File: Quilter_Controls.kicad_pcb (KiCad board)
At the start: 2 copper layers, 40.4 x 110 mm, 16 parts, among them J1 Conn_01x10_Male, J10 Conn_01x04_Male, J2 Conn_01x10_Male, J3 Conn_01x10_Male, J4 Audio_In, J5 Audio_Out, J6 Audio_Mix, J7 Freq_V_Oct, J8 Freq_CV, J9 Conn_02x04_Top_Bottom

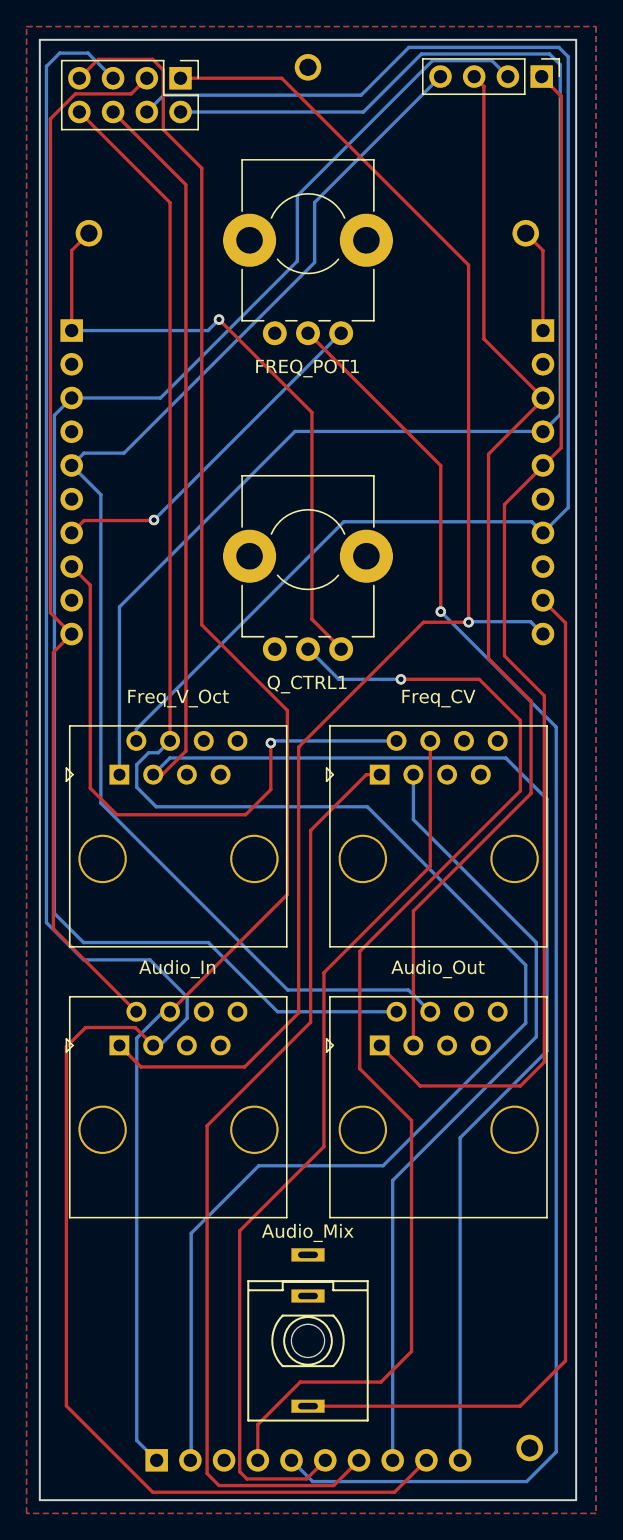
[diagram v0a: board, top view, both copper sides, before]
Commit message: Re-routed Controls board
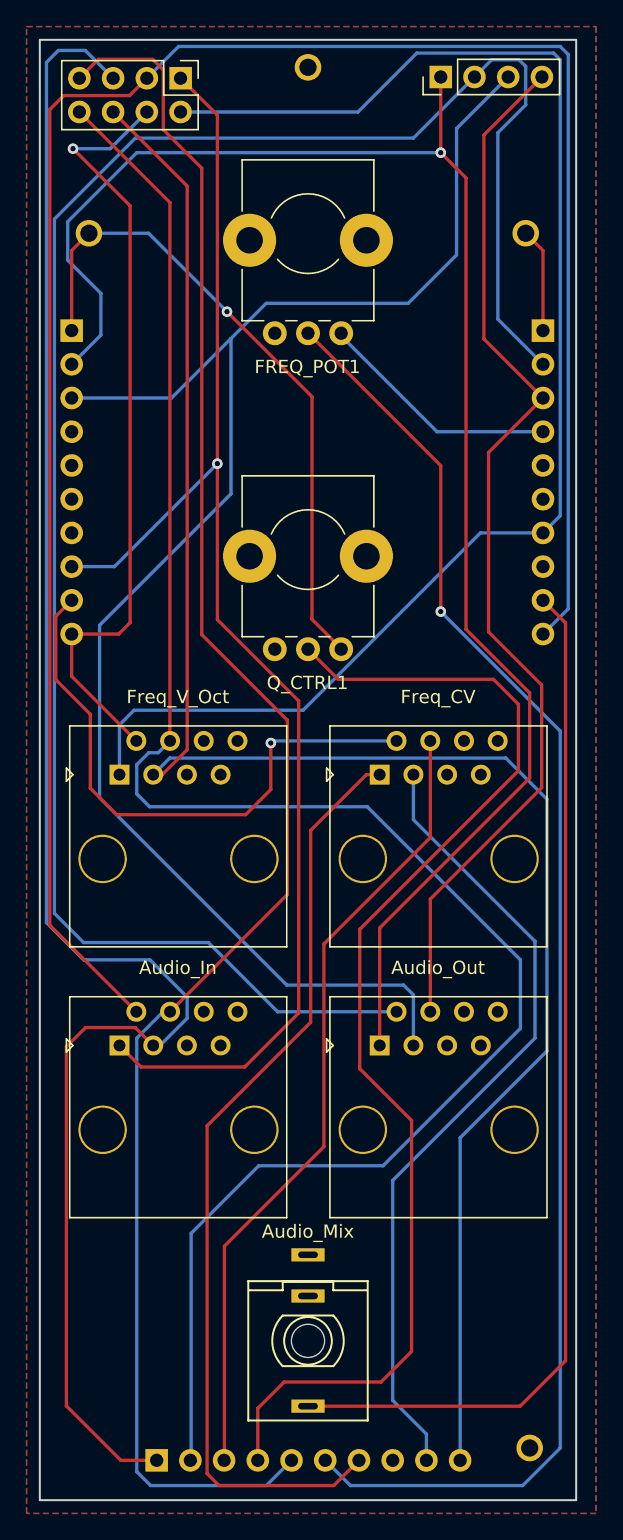
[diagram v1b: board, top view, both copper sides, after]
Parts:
- moved J10 7.60 mm to (80.2, 43.7), turned to 90 degrees
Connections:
- J1 pad 10: /AUDIO_IN1 -> /AUDIO_IN2
- J1 pad 2: unconnected-(J1-Pad2) -> /AUDIO_BUFF2
- J1 pad 3: /AUDIO_BUFF3 -> /AUDIO_BUFF4
- J1 pad 4: /FREQ_V_OCT1 -> /FREQ_POT_5V
- J1 pad 5: /AUDIO_BUFF1 -> unconnected-(J1-Pad5)
- J1 pad 7: /FREQ_V_OCT2 -> /FREQ_V_OCT1
- J2 pad 10: /AUDIO_IN2 -> /FREQ_V_OCT2
- J2 pad 2: unconnected-(J2-Pad2) -> /AUDIO_BUFF1
- J2 pad 3: /AUDIO_BUFF2 -> /AUDIO_BUFF3
- J2 pad 5: /AUDIO_BUFF4 -> unconnected-(J2-Pad5)
- J2 pad 7: /FREQ_POT_5V -> unconnected-(J2-Pad7)
- J2 pad 8: /FREQ_CV2 -> /AUDIO_IN1
- J2 pad 9: unconnected-(J2-Pad9) -> /FREQ_CV2
- J3 pad 1: /AUDIO_IN4 -> /AUDIO_IN3
- J3 pad 3: unconnected-(J3-Pad3) -> /FREQ_CV4
- J3 pad 5: /FREQ_POT -> /AUDIO_IN4
- J3 pad 6: /FREQ_CV4 -> /FREQ_POT
- J3 pad 8: /FREQ_CV3 -> unconnected-(J3-Pad8)
- J3 pad 9: /AUDIO_IN3 -> /FREQ_CV3
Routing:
- net /AUDIO_IN2: track 79.6 -> 156.4 mm
- net /FREQ_V_OCT2: track 109.0 -> 59.0 mm, vias 0 -> 1
- net /AUDIO_BUFF3: track 81.8 -> 120.8 mm
- net /AUDIO_BUFF2: track 115.0 -> 146.5 mm
- net /AUDIO_BUFF1: track 92.3 -> 123.3 mm, vias 0 -> 1
- net /AUDIO_IN3: track 154.2 -> 132.2 mm
- net /AUDIO_BUFF4: track 100.2 -> 80.9 mm
- net /AUDIO_IN4: track 121.5 -> 134.6 mm
- net /AUDIO_IN1: track 113.0 -> 104.1 mm
- net /FREQ_POT_5V: track 26.5 -> 18.4 mm, vias 1 -> 0
- net /FREQ_CV4: track 68.2 -> 60.6 mm
- net /FREQ_POT: track 113.6 -> 111.5 mm
- net +12V: track 47.9 -> 49.6 mm
- net /FREQ_CV2: track 45.5 -> 44.0 mm
- net /Q_POT: track 89.0 -> 90.2 mm, vias 1 -> 0
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
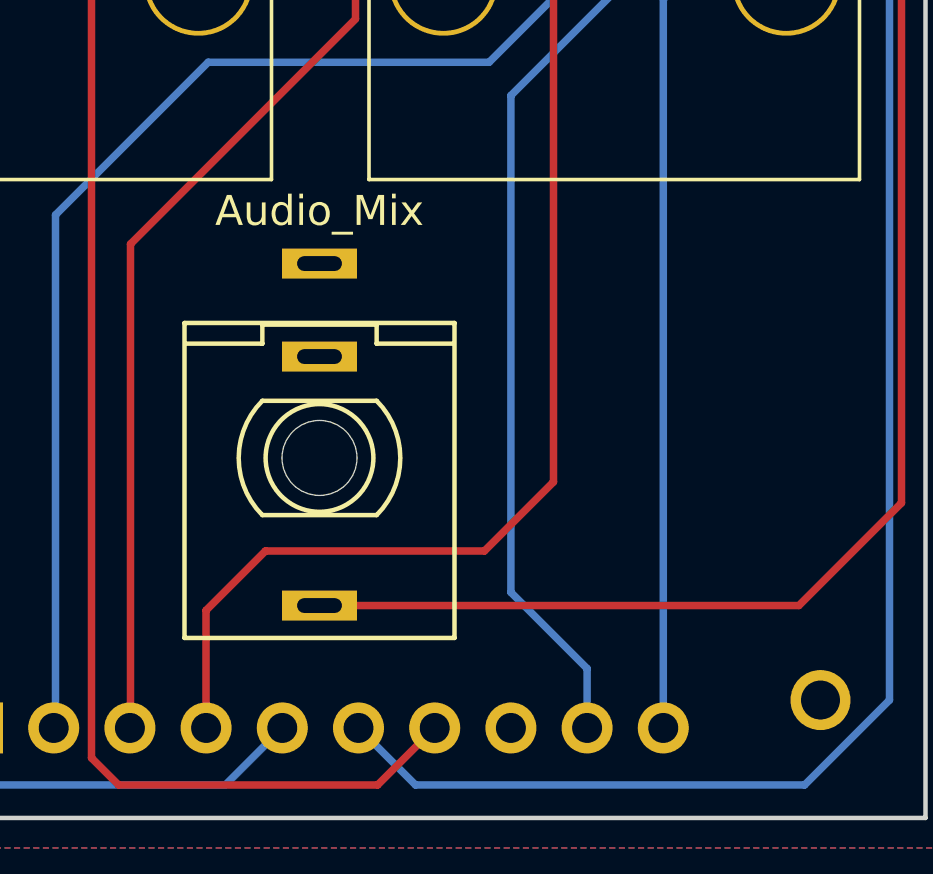
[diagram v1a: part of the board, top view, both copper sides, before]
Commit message: Added all voice filter CV; panel draft done
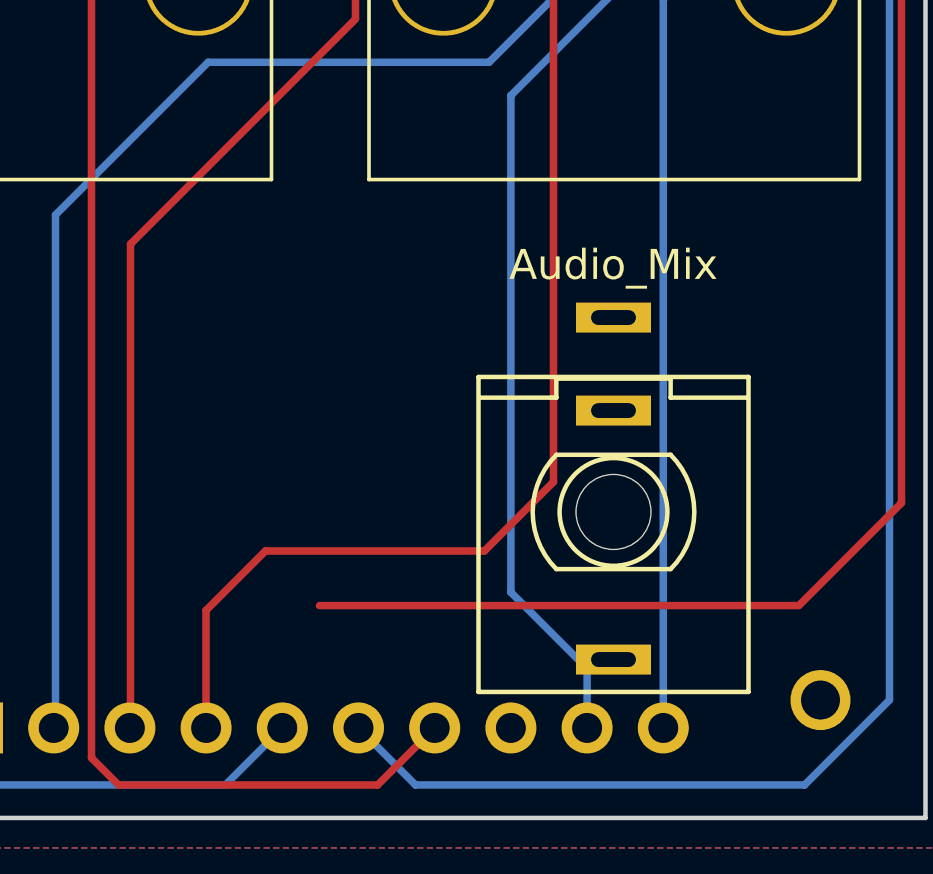
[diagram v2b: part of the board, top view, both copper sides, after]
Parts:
- moved J6 9.96 mm to (80.0, 140.7)
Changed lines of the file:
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@@
   )
   (footprint "Custom_Footprints:THONKICONN_hole" (layer "F.Cu")
-    (at 70.2 138.9 180)
+    (at 80 140.7 180)
     (property "Sheetfile" "Quilter_Controls.kicad_sch")
     (property "Sheetname" "")

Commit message: Updates to panel and component boards
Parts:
- added J11: Freq_In, Custom_Footprints:THONKICONN_hole, F.Cu at (60.4, 140.6)
- J10, J9: moved to B.Cu
- moved J8 30.4 mm to (60.4, 124.1)
- moved J4 26.2 mm to (80.0, 103.9)
- moved Q_CTRL1 10.2 mm to (80.0, 76.6)
- moved FREQ_POT1 5.54 mm to (65.0, 53.6)
- moved J7 3.00 mm to (60.4, 103.9)
- moved J5 2.80 mm to (80.0, 124.1)
- moved J9 2.58 mm to (60.6, 46.4), turned to 90 degrees
- moved J6 0.10 mm to (80.0, 140.6), turned to -90 degrees
- turned J10 to -90 degrees
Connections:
- J3 pad 8: unconnected-(J3-Pad8) -> /FREQ_JACK
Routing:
- net /FREQ_V_OCT3: track 137.7 -> 64.2 mm
- net /AUDIO_IN2: track 156.4 -> 94.4 mm
- net /AUDIO_IN1: track 104.1 -> 45.4 mm, vias 1 -> 0
- net +12V: track 49.6 -> 7.87 mm, vias 1 -> 0
- net /FREQ_CV1: track 71.2 -> 35.9 mm
- net /FREQ_CV4: track 60.6 -> 35.9 mm
- net /FREQ_V_OCT4: track 143.2 -> 118.7 mm
- net /FREQ_CV3: track 60.9 -> 37.0 mm
- net /FREQ_V_OCT1: track 108.5 -> 128.6 mm
- net /Q_POT: track 90.2 -> 70.3 mm
- net /AUDIO_MIX: track 78.8 -> 61.1 mm
- net /FREQ_JACK: track 0.00 -> 16.0 mm
- net /FREQ_CV2: track 44.0 -> 35.8 mm, vias 1 -> 0
- net /AUDIO_BUFF2: track 146.5 -> 153.4 mm
- net /FREQ_POT_5V: track 18.4 -> 24.3 mm
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
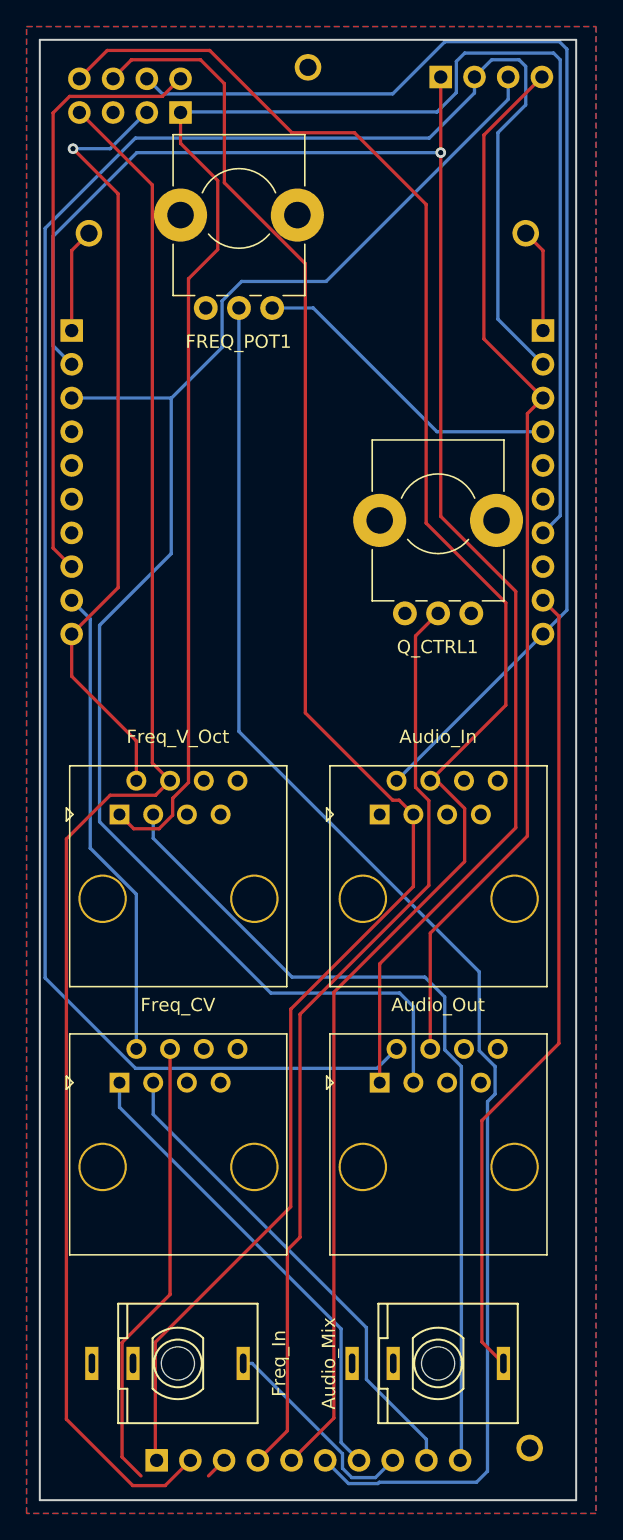
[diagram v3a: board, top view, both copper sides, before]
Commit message: Finished routing components and controls
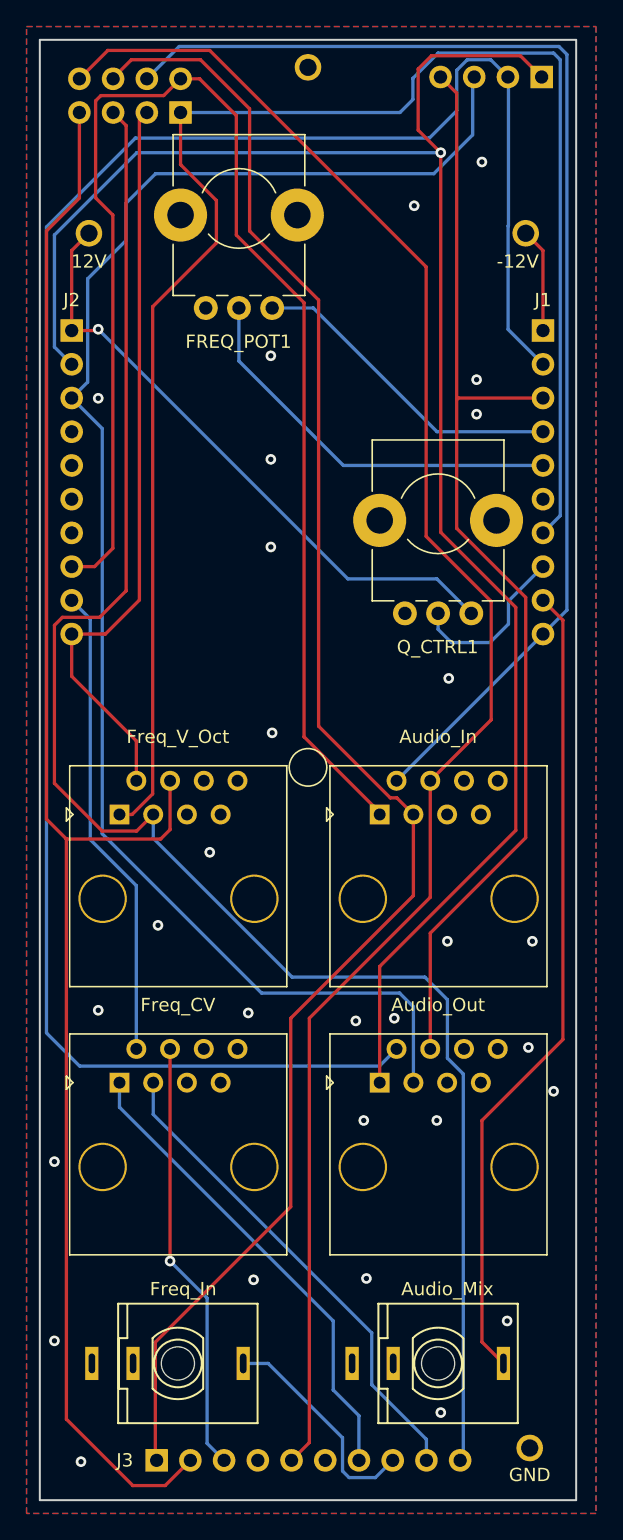
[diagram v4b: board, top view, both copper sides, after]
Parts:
- added D1: 3d_Model_Panel, Custom_Footprints:3D_Dummy, B.Cu at (70.2, 100.0)
- added D2: 3d_Model_Components, Custom_Footprints:3D_Dummy, F.Cu at (70.2, 95.7)
- moved J10 7.60 mm to (87.8, 43.7), turned to 90 degrees
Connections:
- J1 pad 5: unconnected-(J1-Pad5) -> /FREQ_POT
- J1 pad 8: unconnected-(J1-Pad8) -> /Q_POT
- J2 pad 4: unconnected-(J2-Pad4) -> GND
- J2 pad 5: unconnected-(J2-Pad5) -> GND
- J2 pad 7: unconnected-(J2-Pad7) -> GND
- J3 pad 4: /Q_POT -> GND
- J3 pad 6: /FREQ_POT -> GND
- J9 pad 1: /AUDIO_IN1 -> /FREQ_V_OCT1
- J9 pad 2: /FREQ_V_OCT1 -> /AUDIO_IN1
- J9 pad 3: /AUDIO_IN2 -> /FREQ_V_OCT2
- J9 pad 4: /FREQ_V_OCT2 -> /AUDIO_IN2
- J9 pad 5: /AUDIO_IN3 -> /FREQ_V_OCT3
- J9 pad 6: /FREQ_V_OCT3 -> /AUDIO_IN3
- J9 pad 7: /AUDIO_IN4 -> /FREQ_V_OCT4
- J9 pad 8: /FREQ_V_OCT4 -> /AUDIO_IN4
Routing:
- net /FREQ_POT: track 109.2 -> 30.2 mm
- net /FREQ_V_OCT3: track 64.2 -> 128.5 mm
- net /AUDIO_IN1: track 45.4 -> 107.5 mm
- net /Q_POT: track 70.3 -> 12.9 mm
- net +12V: track 7.87 -> 46.9 mm, vias 0 -> 1
- net /AUDIO_BUFF1: track 124.4 -> 136.0 mm
- net /AUDIO_IN4: track 138.0 -> 131.9 mm
- net /FREQ_V_OCT4: track 118.7 -> 124.1 mm
- net /AUDIO_BUFF4: track 80.4 -> 85.4 mm
- net /FREQ_V_OCT1: track 128.6 -> 125.4 mm
- net /FREQ_CV4: track 35.9 -> 32.7 mm, vias 0 -> 1
- net /FREQ_V_OCT2: track 59.2 -> 56.2 mm, vias 1 -> 0
- net /AUDIO_BUFF3: track 115.2 -> 117.3 mm
- net /AUDIO_IN2: track 94.4 -> 92.9 mm
- net /FREQ_JACK: track 16.0 -> 16.8 mm
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- added copper zone on B.Cu, net GND
- added copper zone on F.Cu, net GND
- removed copper zone on B.Cu, net (none)
- removed copper zone on F.Cu, net (none)
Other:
- board text added: "-12V"
- board text added: "1"
- board text added: "12V"
- board text added: "GND"
- board text added: "In"
- board text added: "J1"
- board text added: "J2"
- board text added: "J3"
- board text added: "Out"
- board text added: "V/O"

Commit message: Schematic formatting
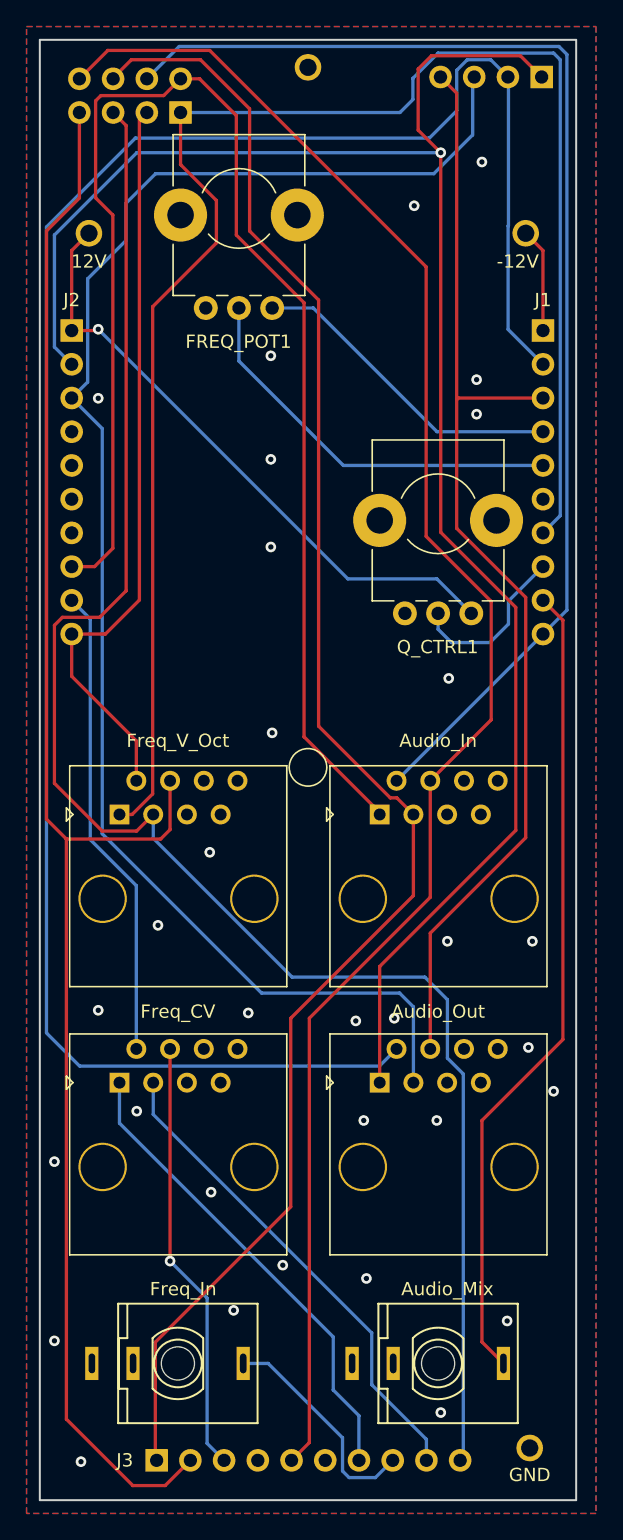
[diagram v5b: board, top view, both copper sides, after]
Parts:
- D1: value 3d_Model_Panel -> 3d_Model_Components
- D2: value 3d_Model_Components -> 3d_Model_Panel
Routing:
- net GND: vias 29 -> 32
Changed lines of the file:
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@@
       (effects (font (size 1 1) (thickness 0.15)))
     )
-    (fp_text value "3d_Model_Components" (at 0 -3 unlocked) (layer "F.Fab")
+    (fp_text value "3d_Model_Panel" (at 0 -3 unlocked) (layer "F.Fab")
       (effects (font (size 1 1) (thickness 0.15)))
     )
@@
       (effects (font (size 1 1) (thickness 0.15)))
     )
-    (fp_text value "Audio_In" (at 0 -10.5) (layer "F.SilkS")
+    (fp_text value "Audio_In" (at 0 -10.2) (layer "F.SilkS")
       (effects (font (size 1 1) (thickness 0.15)))
     )
@@
       (effects (font (size 1 1) (thickness 0.15)))
     )
-    (fp_text value "Audio_Out" (at 0 -10.5) (layer "F.SilkS")
+    (fp_text value "Audio_Out" (at 0 -10) (layer "F.SilkS")
       (effects (font (size 1 1) (thickness 0.15)))
     )
@@
       (effects (font (size 1 1) (thickness 0.15)))
     )
-    (fp_text value "Freq_CV" (at 0 -10.5) (layer "F.SilkS")
+    (fp_text value "Freq_CV" (at 0 -10) (layer "F.SilkS")
       (effects (font (size 1 1) (thickness 0.15)))
     )
@@
       (effects (font (size 1 1) (thickness 0.15)))
     )
-    (fp_text value "Freq_V_Oct" (at 0 -10.5) (layer "F.SilkS")
+    (fp_text value "Freq_V_Oct" (at 0 -10.2) (layer "F.SilkS")
       (effects (font (size 1 1) (thickness 0.15)))
     )
@@
       (effects (font (size 1 1) (thickness 0.15)) (justify mirror))
     )
-    (fp_text value "3d_Model_Panel" (at 0 3 unlocked) (layer "B.Fab")
+    (fp_text value "3d_Model_Components" (at 0 3 unlocked) (layer "B.Fab")
       (effects (font (size 1 1) (thickness 0.15)) (justify mirror))
     )
@@
   (via (at 82.9 66.5) (size 0.8) (drill 0.4) (layers "F.Cu" "B.Cu") (free) (net 1))
   (via (at 54.4 67.9) (size 0.8) (drill 0.4) (layers "F.Cu" "B.Cu") (free) (net 1))
-  (via (at 66.1 134.3) (size 0.8) (drill 0.4) (layers "F.Cu" "B.Cu") (free) (net 1))
+  (via (at 64.6 136.6) (size 0.8) (drill 0.4) (layers "F.Cu" "B.Cu") (free) (net 1))
   (via (at 53.1 148) (size 0.8) (drill 0.4) (layers "F.Cu" "B.Cu") (free) (net 1))
   (via (at 78.2 53.4) (size 0.8) (drill 0.4) (layers "F.Cu" "B.Cu") (free) (net 1))
@@
   (via (at 74.4 122.3) (size 0.8) (drill 0.4) (layers "F.Cu" "B.Cu") (free) (net 1))
   (via (at 67.5 93.1) (size 0.8) (drill 0.4) (layers "F.Cu" "B.Cu") (free) (net 1))
+  (via (at 62.9 127.7) (size 0.8) (drill 0.4) (layers "F.Cu" "B.Cu") (free) (net 1))
+  (via (at 68.3 133.2) (size 0.8) (drill 0.4) (layers "F.Cu" "B.Cu") (free) (net 1))
   (via (at 51.1 125.4) (size 0.8) (drill 0.4) (layers "F.Cu" "B.Cu") (free) (net 1))
   (via (at 79.9 122.3) (size 0.8) (drill 0.4) (layers "F.Cu" "B.Cu") (free) (net 1))
+  (via (at 57.3 121.6) (size 0.8) (drill 0.4) (layers "F.Cu" "B.Cu") (free) (net 1))
   (via (at 80.2 144.3) (size 0.8) (drill 0.4) (layers "F.Cu" "B.Cu") (free) (net 1))
   (via (at 67.4 72.5) (size 0.8) (drill 0.4) (layers "F.Cu" "B.Cu") (free) (net 1))
@@
   (segment (start 79.41 96.71) (end 79.41 105.49) (width 0.25) (layer "F.Cu") (net 18))
   (segment (start 70.3 146.56) (end 68.96 147.9) (width 0.25) (layer "F.Cu") (net 18))
+  (segment (start 74.04 144.54) (end 72.1 142.6) (width 0.25) (layer "B.Cu") (net 19))
+  (segment (start 72.1 138.6) (end 56 122.5) (width 0.25) (layer "B.Cu") (net 19))
+  (segment (start 56 122.5) (end 56 119.45) (width 0.25) (layer "B.Cu") (net 19))
   (segment (start 74.04 147.9) (end 74.04 144.54) (width 0.25) (layer "B.Cu") (net 19))
-  (segment (start 72.1 137.4) (end 56 121.3) (width 0.25) (layer "B.Cu") (net 19))
-  (segment (start 72.1 142.6) (end 72.1 137.4) (width 0.25) (layer "B.Cu") (net 19))
-  (segment (start 74.04 144.54) (end 72.1 142.6) (width 0.25) (layer "B.Cu") (net 19))
-  (segment (start 56 121.3) (end 56 119.45) (width 0.25) (layer "B.Cu") (net 19))
+  (segment (start 72.1 142.6) (end 72.1 138.6) (width 0.25) (layer "B.Cu") (net 19))
   (segment (start 75 138.3) (end 58.54 121.84) (width 0.25) (layer "B.Cu") (net 20))
   (segment (start 79.12 146.32) (end 75 142.2) (width 0.25) (layer "B.Cu") (net 20))
